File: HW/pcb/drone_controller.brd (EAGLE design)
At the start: 115.6 x 83.8 mm, 29 parts, among them IC2 MEGA8-P, J1 DCJ0202, Q1 16Mhz, U1 ICM-20600

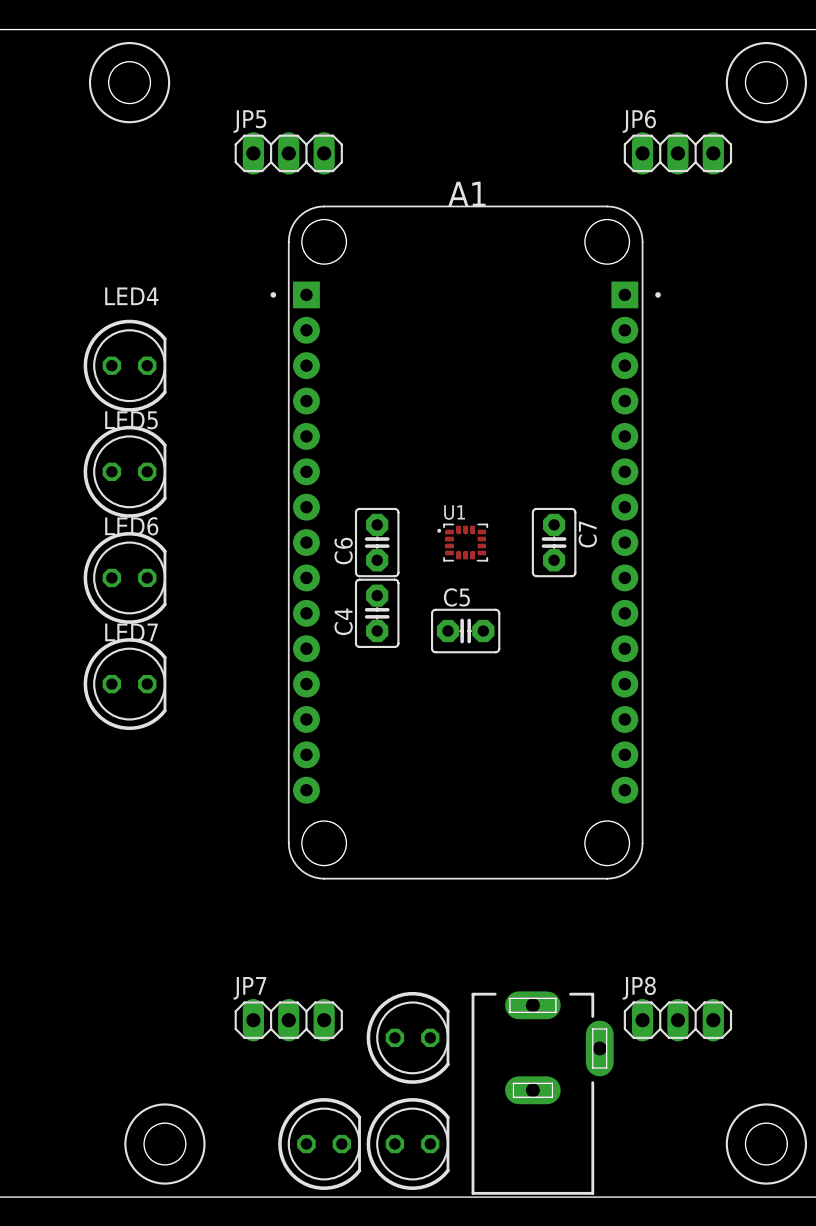
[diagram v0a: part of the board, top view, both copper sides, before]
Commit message: implemented heartbeat LED in SW. Adjusted position of MCU on board to account for loss from GND plane. Removed unneeded battery indicators (only one LED for Low BATT).
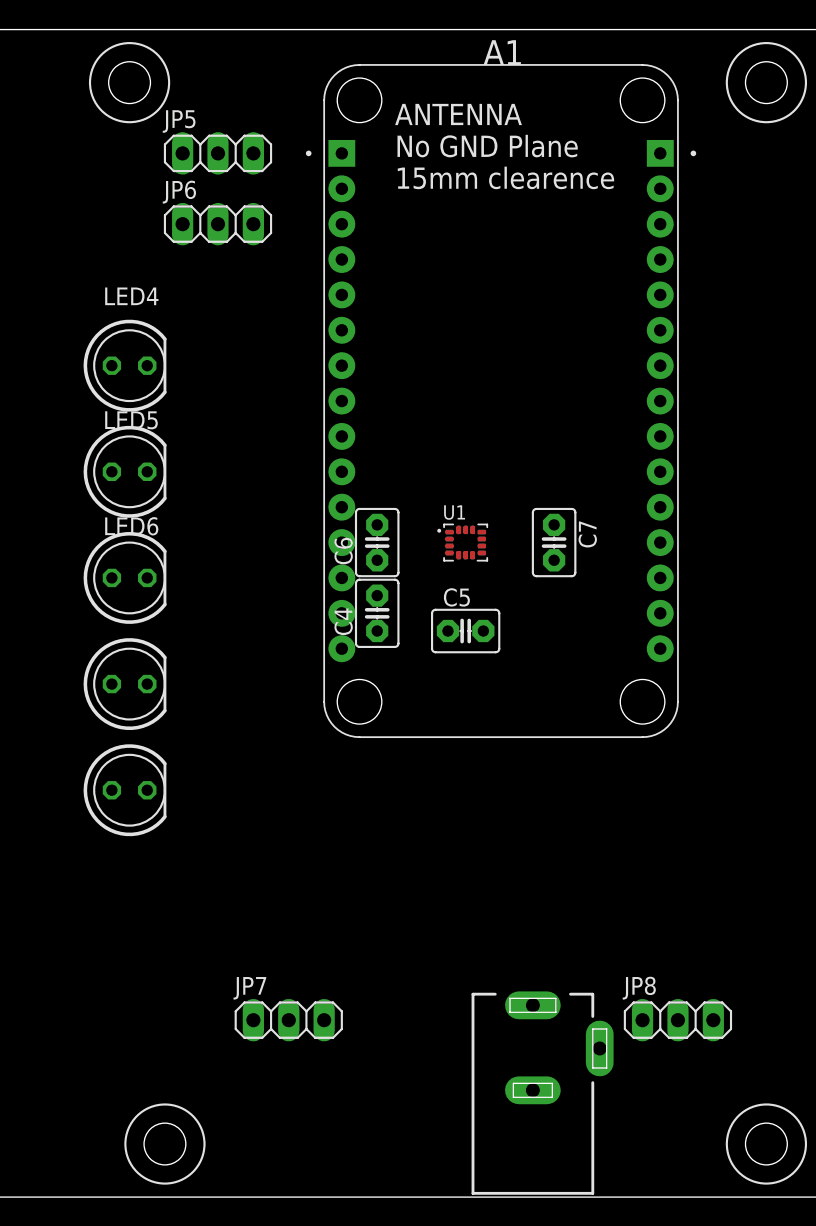
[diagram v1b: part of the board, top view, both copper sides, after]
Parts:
- removed LED1, LED7: (no value), led:LED5MM
- moved LED2 35.9 mm to (64.8, 36.8)
- moved JP6 33.4 mm to (71.1, 69.8)
- moved LED3 27.0 mm to (64.8, 29.2)
- moved A1 10.5 mm to (91.4, 57.1)
- moved JP5 5.08 mm to (71.1, 74.9)
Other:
- board text added: "ANTENNA No GND Plane 15mm clearence"
- board text added: "Batt Low"
- board text added: "WiFi"
- board text removed: "CONN"

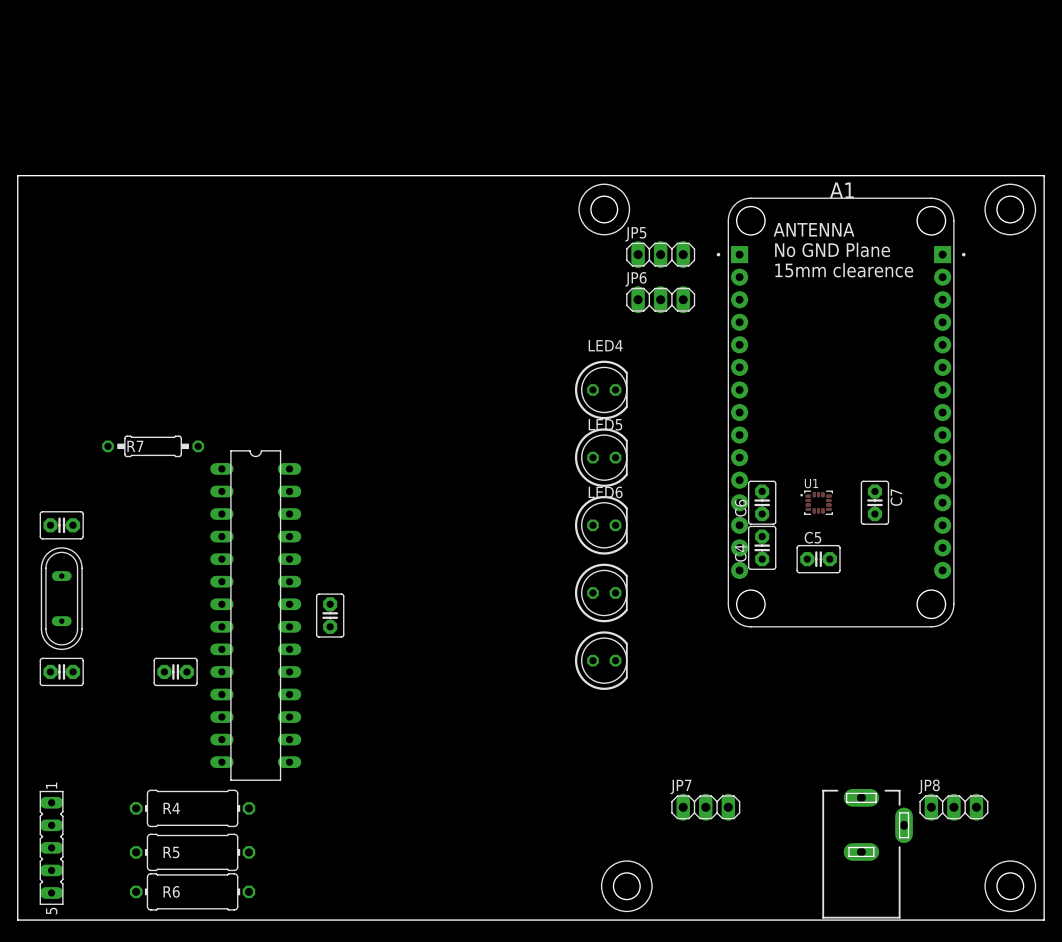
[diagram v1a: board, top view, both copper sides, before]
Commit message: implemented pinout into schematic. added LED interface
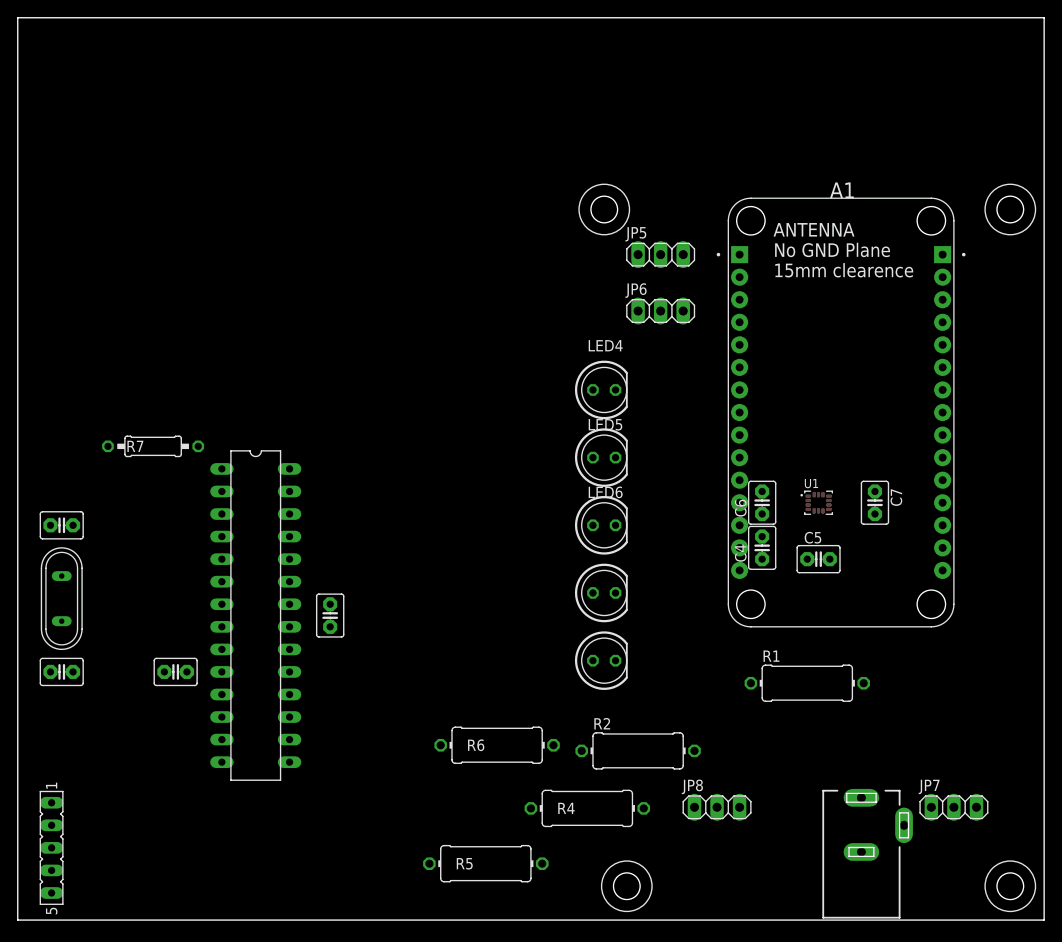
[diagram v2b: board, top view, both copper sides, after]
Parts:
- added R1, R2: 10R, rcl:0411/12
- R4, R5, R6: value 200R -> 10R
- moved R4 44.5 mm to (62.9, 12.6)
- moved R6 38.1 mm to (52.7, 19.7)
- moved R5 33.0 mm to (51.4, 6.35)
- moved JP7 27.9 mm to (104.1, 12.7)
- moved JP8 26.7 mm to (77.5, 12.7)
- moved JP6 1.27 mm to (71.1, 68.6)
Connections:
- net ESC_FLM renamed PWM_MOTOR_FL
- net ESC_FRM renamed PWM_MOTOR_FR
- net ESC_RRM renamed PWM_MOTOR_RL
- removed net ESC_RLM: A1.J2_3, JP7.2
- new net GPIO_LED_HEARTBEAT: A1.J2_4, LED4.A
- new net GPIO_LED_WIFI_CONN: A1.J2_10, LED5.A
- new net GPIO_LED_WIFI_RX: A1.J2_5, LED6.A
- new net LED_BATT_LOW: LED3.A
- new net LED_IMU: LED2.A
- new net N$10: LED4.K, R2.1
- new net N$14: LED6.K, R1.1
- new net N$7: LED2.K, R6.1
- new net N$8: LED3.K, R5.1
- new net N$9: LED5.K, R4.1
- new net PWM_MOTOR_RR: A1.J2_1, JP7.2
- net 3V3: no longer A1.J1_12
- net GND: now also R1.2, R2.2, R4.2, R5.2, R6.2; no longer A1.J1_13
- net SDA: now also A1.J2_3; no longer A1.J2_5
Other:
- board size 115.6 x 83.8 mm -> 115.6 x 101.6 mm

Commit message: working on PCB design. added 3.3v to 5v level shifter, but it is not needed. tested NodeMCU to SpeedyBee ESC and was able to communicate using Servo Library without needed PWM voltage to increase from 3.3v to 5v. 3.3 worked fine.
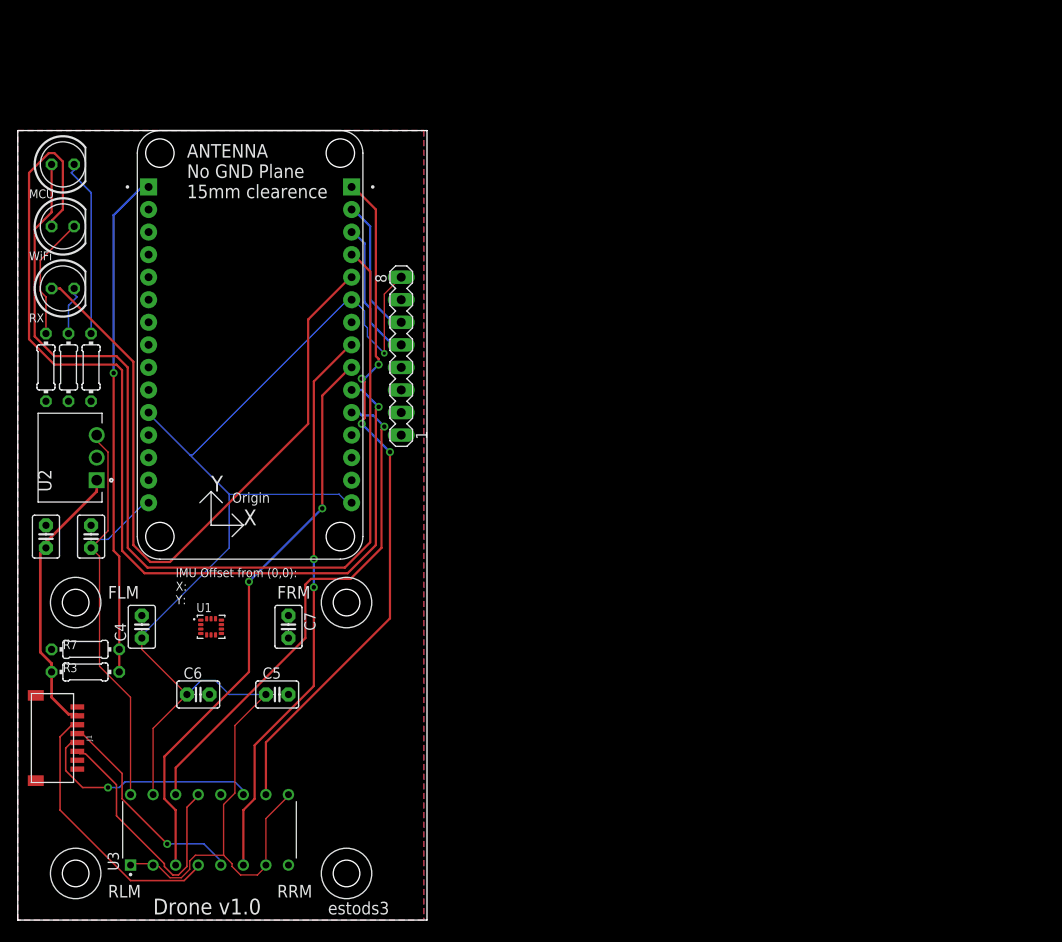
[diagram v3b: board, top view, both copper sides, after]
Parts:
- removed C3: 22pF, capacitor-wima:C2.5-3
- removed C8: 0.1uF, capacitor-wima:C2.5-3
- removed IC2: MEGA8-P, atmel:DIL28-3
- removed JP5, JP6, JP7, JP8: (no value), pinhead:1X03
- removed LED2, LED3: (no value), led:LED5MM
- removed Q1: 16Mhz, special:QS
- removed R4, R5, R6: 10R, rcl:0411/12
- removed SV1: (no value), con-lsta:FE05-1
- added R3: 10k, rcl:0204/7
- added R8: 10R, rcl:0204/7
- added SV2: (no value), con-lstb:MA08-1
- added U2: VXO7805-500, VXO7805-500:CONV_VXO7805-500
- added U3: CD40109BE, CD40109BE:DIP794W45P254L1969H508Q16
- C1: value 0.1uF -> 10uF
- C2: value 22pF -> 22uF
- J1: value DCJ0202 -> SM08B-SRSS-TB; device con-jack:DCJ0202 -> con-JST-SH:SM08B-SRSS-TB
- R1, R2: device rcl:0411/12 -> rcl:0204/7
- R7: value 10k -> 3.3k; device rcl:0207/10 -> rcl:0204/7
- moved J1 93.5 mm to (0.76, 20.5), turned to 270 degrees
- moved R1 92.8 mm to (1.91, 62.2), turned to 270 degrees
- moved R2 77.3 mm to (4.45, 62.2), turned to 270 degrees
- moved C4 70.4 mm to (12.7, 33.0)
- moved U1 69.8 mm to (20.5, 33.0)
- moved C7 67.5 mm to (29.2, 33.0)
- moved C6 67.1 mm to (19.1, 25.4), turned to 0 degrees
- moved A1 67.0 mm to (24.9, 64.8)
- moved LED6 66.5 mm to (3.81, 71.1)
- moved LED5 66.3 mm to (3.81, 78.1)
- moved LED4 66.0 mm to (3.81, 85.1)
- moved C5 62.8 mm to (27.9, 25.4)
- moved C1 33.2 mm to (1.91, 43.2)
- moved R7 24.1 mm to (6.35, 30.5)
- moved C2 3.54 mm to (6.99, 43.2), turned to 90 degrees
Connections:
- removed net LED_BATT_LOW: LED3.A
- removed net LED_IMU: LED2.A
- removed net N$12: C2.1, IC2.9, Q1.2
- removed net N$13: C1.1, IC2.21
- removed net N$7: LED2.K, R6.1
- removed net N$8: LED3.K, R5.1
- removed net RESET: IC2.1, R7.2, SV1.4
- removed net RX: IC2.2, SV1.2
- removed net TX: IC2.3, SV1.3
- new net CURR: J1.7
- new net GPIO_BATT_SOC: A1.J1_1, R3.1, R7.2
- new net INT: SV2.1
- new net N$17: SV2.4
- new net N$18: SV2.3
- new net N$19: SV2.2
- new net N$2: J1.3, U3.4
- new net N$3: J1.4, U3.5
- new net N$4: J1.5, U3.11
- new net TEL: J1.8
- net 3V3: now also SV2.8, U3.1, U3.15, U3.2, U3.7, U3.9
- net 5V: now also C2.1, U2.3, U3.16; no longer C8.2, IC2.20, IC2.7, R7.1, SV1.1
- net GND: now also J1.1, R7.1, R8.2, SV2.7, U2.2, U3.8; no longer C3.2, C8.1, IC2.22, IC2.8, J1.2, J1.3, JP5.3, JP6.3, JP7.3, JP8.3, R4.2, R5.2, R6.2, SV1.5
- net N$10: now also R8.1; no longer R2.1
- net N$11: now also J1.6, U3.13; no longer C3.1, IC2.10, Q1.1
- net N$14: now also R2.1; no longer R1.1
- net N$9: now also R1.1; no longer R4.1
- net PWM_MOTOR_FL: now also U3.6; no longer JP5.2
- net PWM_MOTOR_FR: now also U3.3; no longer JP6.2
- net PWM_MOTOR_RL: now also U3.14; no longer JP8.2
- net PWM_MOTOR_RR: now also U3.10; no longer JP7.2
- net SCL: now also SV2.6
- net SDA: now also SV2.5
- net VCC: now also C1.1, J1.2, R3.2, U2.1; no longer J1.1, JP5.1, JP6.1, JP7.1, JP8.1
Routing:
- net 3V3: track 0.00 -> 170.1 mm, vias 0 -> 1
- net GPIO_LED_HEARTBEAT: track 0.00 -> 115.2 mm
- net GPIO_LED_WIFI_CONN: track 0.00 -> 114.4 mm, vias 0 -> 1
- net GPIO_LED_WIFI_RX: track 0.00 -> 78.8 mm
- net PWM_MOTOR_RR: track 0.00 -> 78.1 mm, vias 0 -> 4
- net PWM_MOTOR_FR: track 0.00 -> 65.4 mm, vias 0 -> 2
- net PWM_MOTOR_FL: track 0.00 -> 63.7 mm, vias 0 -> 2
- net PWM_MOTOR_RL: track 0.00 -> 58.1 mm, vias 0 -> 1
- net GPIO_BATT_SOC: track 0.00 -> 57.0 mm, vias 0 -> 1
- net 5V: track 0.00 -> 52.2 mm
- net VCC: track 0.00 -> 31.4 mm
- net N$2: track 0.00 -> 30.4 mm
- net N$11: track 0.00 -> 29.4 mm
- net N$4: track 0.00 -> 26.0 mm, vias 0 -> 1
- net N$3: track 0.00 -> 24.2 mm, vias 0 -> 1
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- added copper zone on layer 1, net GND
- added copper zone on layer 16, net GND
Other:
- board size 115.6 x 101.6 mm -> 46.1 x 88.9 mm
- board text added: "IMU Offset from (0,0): X: Y:"
- board text added: "Origin"
- board text added: "X"
- board text added: "Y"
- board text added: "estods3"
- board text removed: "Batt Low"
- board text removed: "IMU"
